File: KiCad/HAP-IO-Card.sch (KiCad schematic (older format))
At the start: 0 parts

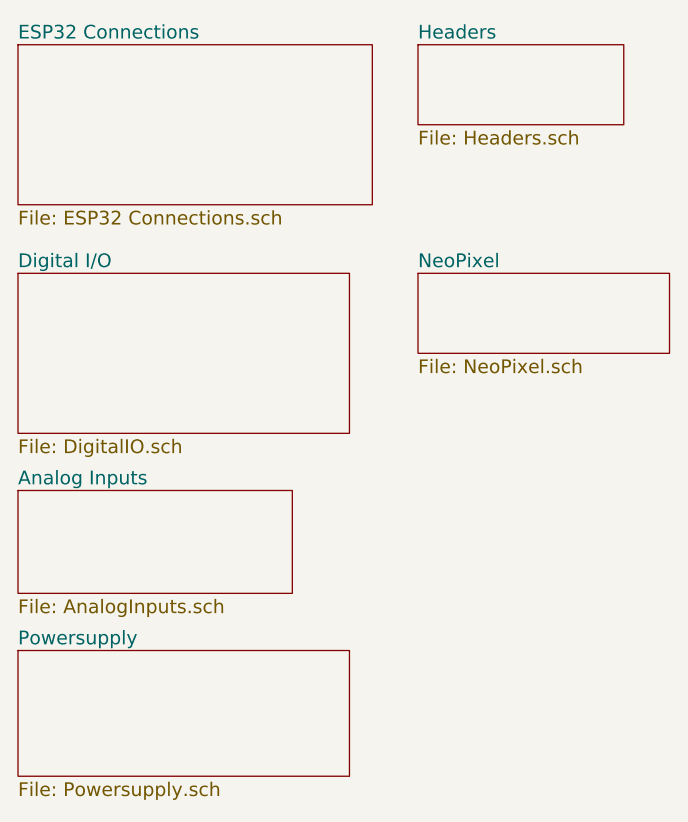
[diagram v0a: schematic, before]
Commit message: Save with sensor inputs using digital potentiometer
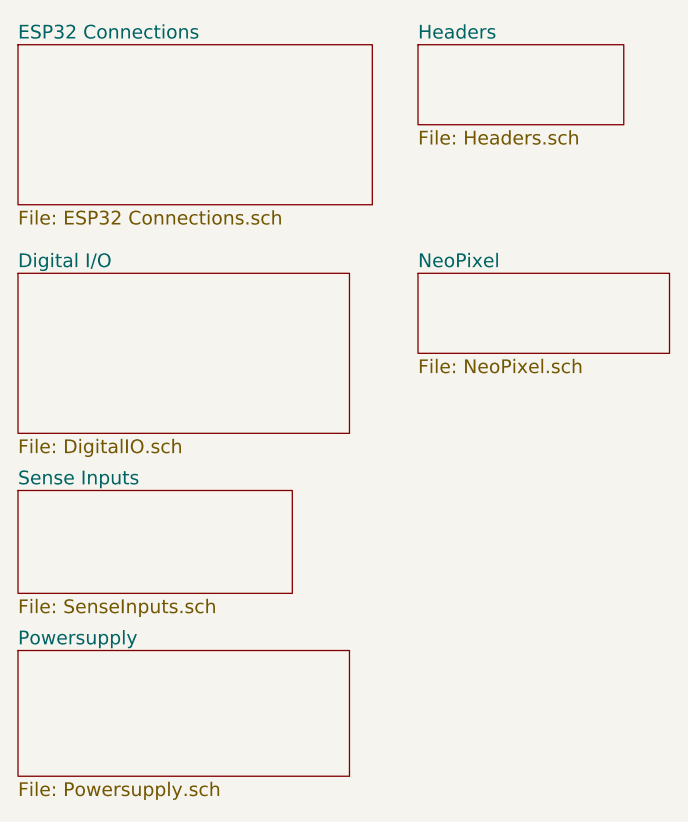
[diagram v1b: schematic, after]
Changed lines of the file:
@@
 LIBS:ADS1115IDGST
 LIBS:LM1086
+LIBS:X95840WV20IZ-2_7T1
+LIBS:804-112
 LIBS:HAP-IO-Card-cache
 EELAYER 26 0
@@
 S 900  2750 1200 450
 U 591A7DC8
-F0 "Analog Inputs" 60
-F1 "AnalogInputs.sch" 60
+F0 "Sense Inputs" 60
+F1 "SenseInputs.sch" 60
 $EndSheet
 $Sheet
